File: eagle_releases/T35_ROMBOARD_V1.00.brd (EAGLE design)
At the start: 80 x 61 mm, 10 parts

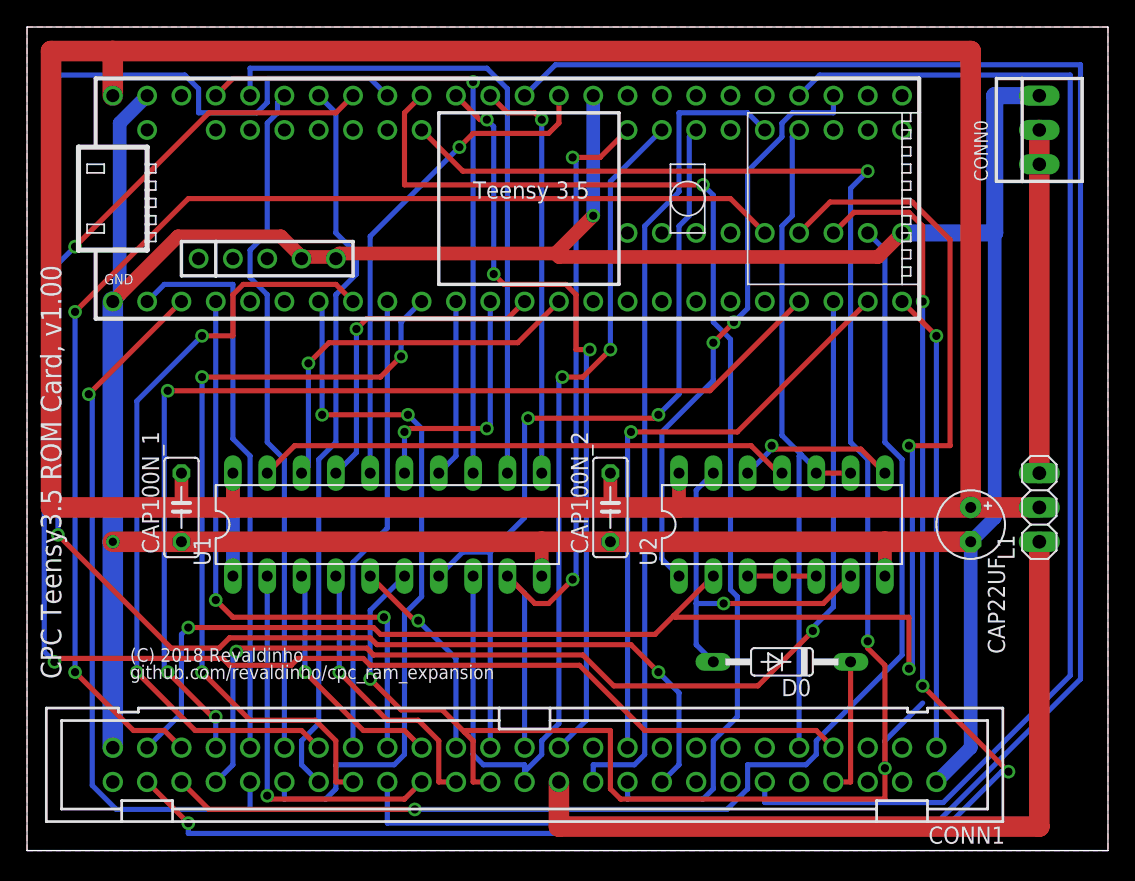
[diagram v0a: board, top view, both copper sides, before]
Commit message: Updates to Teensy 3.5 ROM board
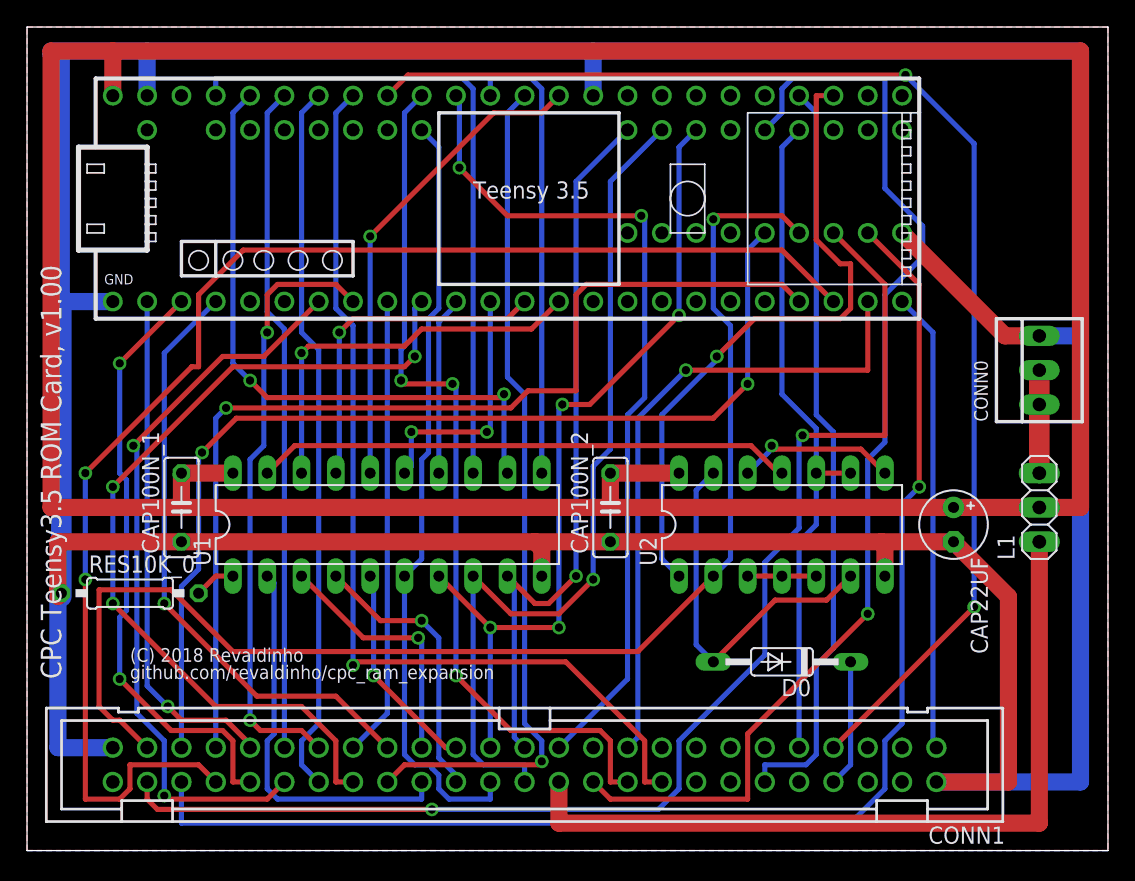
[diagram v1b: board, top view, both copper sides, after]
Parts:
- added RES10K_0: (no value), resistor:0207/10
- moved CONN0 17.8 mm to (74.9, 35.6)
- moved CAP22UF 1.27 mm to (68.6, 24.1)
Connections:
- new net VSS_PULLDOWN: RES10K_0.2, U1.1
- net VDD: no longer U1.1
- net VSS: now also RES10K_0.1; no longer U0.GND1, U0.GND4
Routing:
- net D3: track 146.6 -> 57.5 mm, vias 4 -> 0
- net A1: track 146.3 -> 62.9 mm, vias 0 -> 1
- net VSS: track 266.1 -> 324.9 mm, vias 2 -> 0
- net RAMRD_B: track 134.9 -> 95.2 mm, vias 1 -> 2
- net READY: track 93.2 -> 55.7 mm
- net WR_B: track 105.6 -> 71.6 mm, vias 3 -> 1
- net A15: track 118.3 -> 94.2 mm, vias 4 -> 2
- net A14: track 120.6 -> 97.6 mm, vias 3 -> 1
- net M1_B: track 60.8 -> 83.3 mm, vias 0 -> 1
- net A11: track 80.9 -> 103.3 mm
- net IOREQ_B: track 83.7 -> 65.1 mm, vias 1 -> 3
- net VDD_EXT: track 25.4 -> 7.62 mm
- net A12: track 92.4 -> 76.7 mm
- net A4: track 57.7 -> 45.1 mm
- net A9: track 53.2 -> 44.8 mm, vias 1 -> 2
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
